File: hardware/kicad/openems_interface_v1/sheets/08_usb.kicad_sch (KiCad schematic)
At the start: 1 part, among them U5 ADuM3160_class

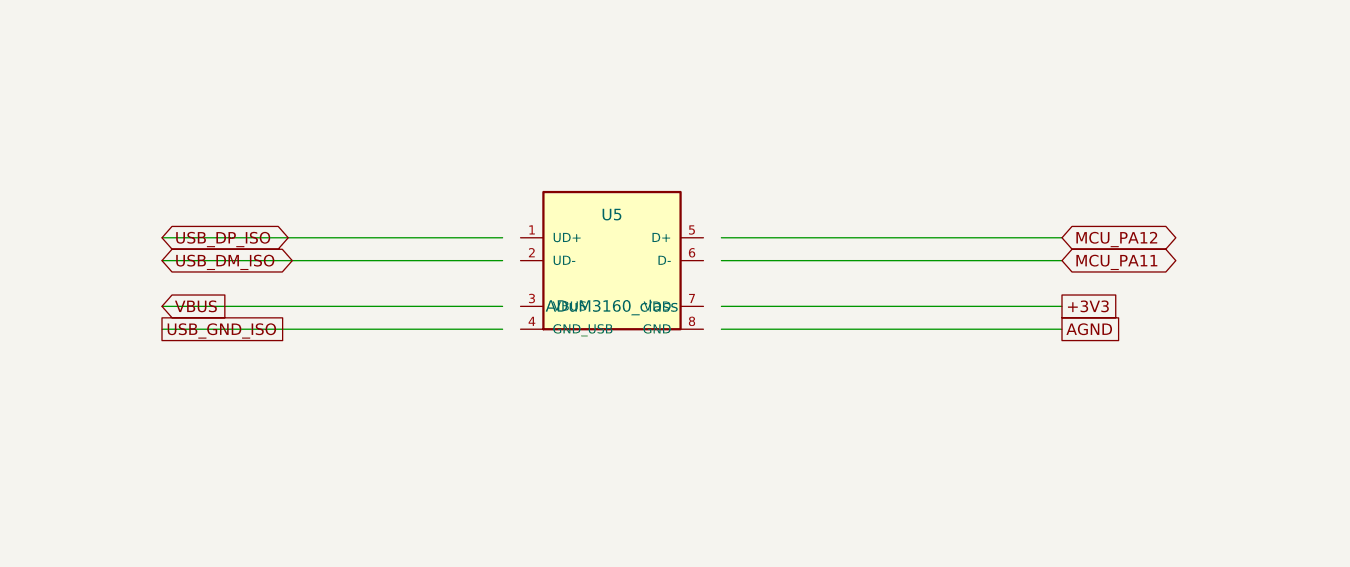
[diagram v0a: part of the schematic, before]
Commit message: feat(hw): nets J1/J2 no PCB + zones PGND + star GND no sch
Atribui pads AMPSEAL a partir de pinmap_logical.md (autoridade),
adiciona pours PGND F/B, e evita curto de terras no esquemático
(star só via NetTie no layout). Script annotate_pcb_nets.py.
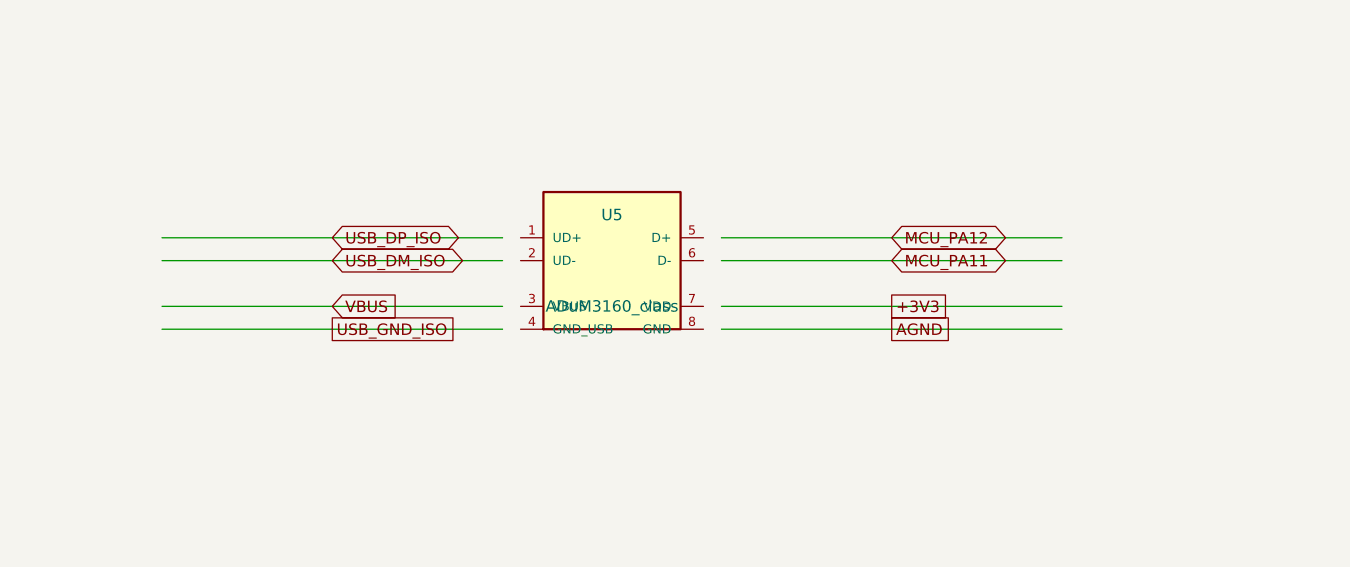
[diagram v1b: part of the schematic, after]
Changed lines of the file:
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@@
     (pin "8")
   )
-  (global_label "USB_DP_ISO" (shape bidirectional) (at 90 97.46 0) (fields_autoplaced)
+  (wire (pts (xy 127.84 97.46) (xy 90 97.46))
+    (stroke (width 0) (type default))
+  )
+  (global_label "USB_DP_ISO" (shape bidirectional) (at 108.92 97.46 180) (fields_autoplaced)
     (effects (font (size 1.27 1.27)) (justify left))
-    (property "Intersheetrefs" "${INTERSHEET_REFS}" (at 90 97.46 0)
+    (property "Intersheetrefs" "${INTERSHEET_REFS}" (at 108.92 97.46 0)
       (effects (font (size 1.27 1.27)) hide)
     )
   )
-  (wire (pts (xy 90 97.46) (xy 127.84 97.46))
+  (wire (pts (xy 127.84 100) (xy 90 100))
     (stroke (width 0) (type default))
   )
-  (global_label "USB_DM_ISO" (shape bidirectional) (at 90 100 0) (fields_autoplaced)
+  (global_label "USB_DM_ISO" (shape bidirectional) (at 108.92 100 180) (fields_autoplaced)
     (effects (font (size 1.27 1.27)) (justify left))
-    (property "Intersheetrefs" "${INTERSHEET_REFS}" (at 90 100 0)
+    (property "Intersheetrefs" "${INTERSHEET_REFS}" (at 108.92 100 0)
       (effects (font (size 1.27 1.27)) hide)
     )
   )
-  (wire (pts (xy 90 100) (xy 127.84 100))
+  (wire (pts (xy 127.84 105.08) (xy 90 105.08))
     (stroke (width 0) (type default))
   )
-  (global_label "VBUS" (shape input) (at 90 105.08 0) (fields_autoplaced)
+  (global_label "VBUS" (shape input) (at 108.92 105.08 180) (fields_autoplaced)
     (effects (font (size 1.27 1.27)) (justify left))
-    (property "Intersheetrefs" "${INTERSHEET_REFS}" (at 90 105.08 0)
+    (property "Intersheetrefs" "${INTERSHEET_REFS}" (at 108.92 105.08 0)
       (effects (font (size 1.27 1.27)) hide)
     )
   )
-  (wire (pts (xy 90 105.08) (xy 127.84 105.08))
+  (wire (pts (xy 127.84 107.62) (xy 90 107.62))
     (stroke (width 0) (type default))
   )
-  (global_label "USB_GND_ISO" (shape passive) (at 90 107.62 0) (fields_autoplaced)
+  (global_label "USB_GND_ISO" (shape passive) (at 108.92 107.62 180) (fields_autoplaced)
     (effects (font (size 1.27 1.27)) (justify left))
-    (property "Intersheetrefs" "${INTERSHEET_REFS}" (at 90 107.62 0)
+    (property "Intersheetrefs" "${INTERSHEET_REFS}" (at 108.92 107.62 0)
       (effects (font (size 1.27 1.27)) hide)
     )
   )
-  (wire (pts (xy 90 107.62) (xy 127.84 107.62))
+  (wire (pts (xy 152.16 97.46) (xy 190 97.46))
     (stroke (width 0) (type default))
   )
-  (global_label "MCU_PA12" (shape bidirectional) (at 190 97.46 0) (fields_autoplaced)
+  (global_label "MCU_PA12" (shape bidirectional) (at 171.07999999999998 97.46 180) (fields_autoplaced)
     (effects (font (size 1.27 1.27)) (justify left))
-    (property "Intersheetrefs" "${INTERSHEET_REFS}" (at 190 97.46 0)
+    (property "Intersheetrefs" "${INTERSHEET_REFS}" (at 171.07999999999998 97.46 0)
       (effects (font (size 1.27 1.27)) hide)
     )
   )
-  (wire (pts (xy 190 97.46) (xy 152.16 97.46))
+  (wire (pts (xy 152.16 100) (xy 190 100))
     (stroke (width 0) (type default))
   )
-  (global_label "MCU_PA11" (shape bidirectional) (at 190 100 0) (fields_autoplaced)
+  (global_label "MCU_PA11" (shape bidirectional) (at 171.07999999999998 100 180) (fields_autoplaced)
     (effects (font (size 1.27 1.27)) (justify left))
-    (property "Intersheetrefs" "${INTERSHEET_REFS}" (at 190 100 0)
+    (property "Intersheetrefs" "${INTERSHEET_REFS}" (at 171.07999999999998 100 0)
       (effects (font (size 1.27 1.27)) hide)
     )
   )
-  (wire (pts (xy 190 100) (xy 152.16 100))
+  (wire (pts (xy 152.16 105.08) (xy 190 105.08))
     (stroke (width 0) (type default))
   )
-  (global_label "+3V3" (shape passive) (at 190 105.08 0) (fields_autoplaced)
+  (global_label "+3V3" (shape passive) (at 171.07999999999998 105.08 180) (fields_autoplaced)
     (effects (font (size 1.27 1.27)) (justify left))
-    (property "Intersheetrefs" "${INTERSHEET_REFS}" (at 190 105.08 0)
+    (property "Intersheetrefs" "${INTERSHEET_REFS}" (at 171.07999999999998 105.08 0)
       (effects (font (size 1.27 1.27)) hide)
     )
   )
-  (wire (pts (xy 190 105.08) (xy 152.16 105.08))
+  (wire (pts (xy 152.16 107.62) (xy 190 107.62))
     (stroke (width 0) (type default))
   )
-  (global_label "AGND" (shape passive) (at 190 107.62 0) (fields_autoplaced)
+  (global_label "AGND" (shape passive) (at 171.07999999999998 107.62 180) (fields_autoplaced)
     (effects (font (size 1.27 1.27)) (justify left))
-    (property "Intersheetrefs" "${INTERSHEET_REFS}" (at 190 107.62 0)
+    (property "Intersheetrefs" "${INTERSHEET_REFS}" (at 171.07999999999998 107.62 0)
       (effects (font (size 1.27 1.27)) hide)
     )
   )
-  (wire (pts (xy 190 107.62) (xy 152.16 107.62))
-    (stroke (width 0) (type default))
-  )
   (text "USB conector no edge. ESD TVS em D+/D− lado host.\\nUSB_GND_ISO isolado de PGND (sem pour por baixo da barreira)." (at 50.8 150 0)
